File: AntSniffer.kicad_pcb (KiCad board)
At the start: 4 copper layers, 50.1 x 30.1 mm, 6 parts, among them CN1 X2026WRS-2X09D-LPSW, CN2 X2026WRS-2X09D-LPSW, J1 Conn_01x10_MountingPin

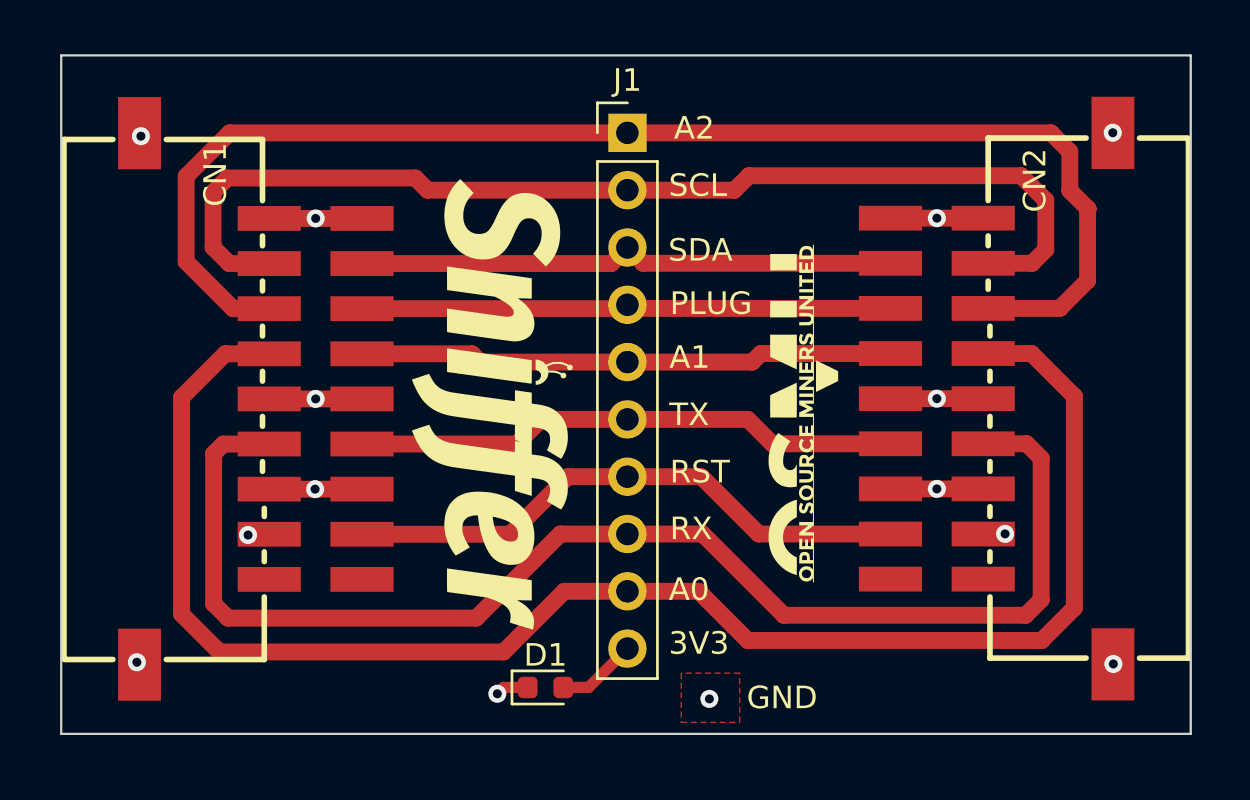
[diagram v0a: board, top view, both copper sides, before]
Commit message: switched to two layer board. added GND pin
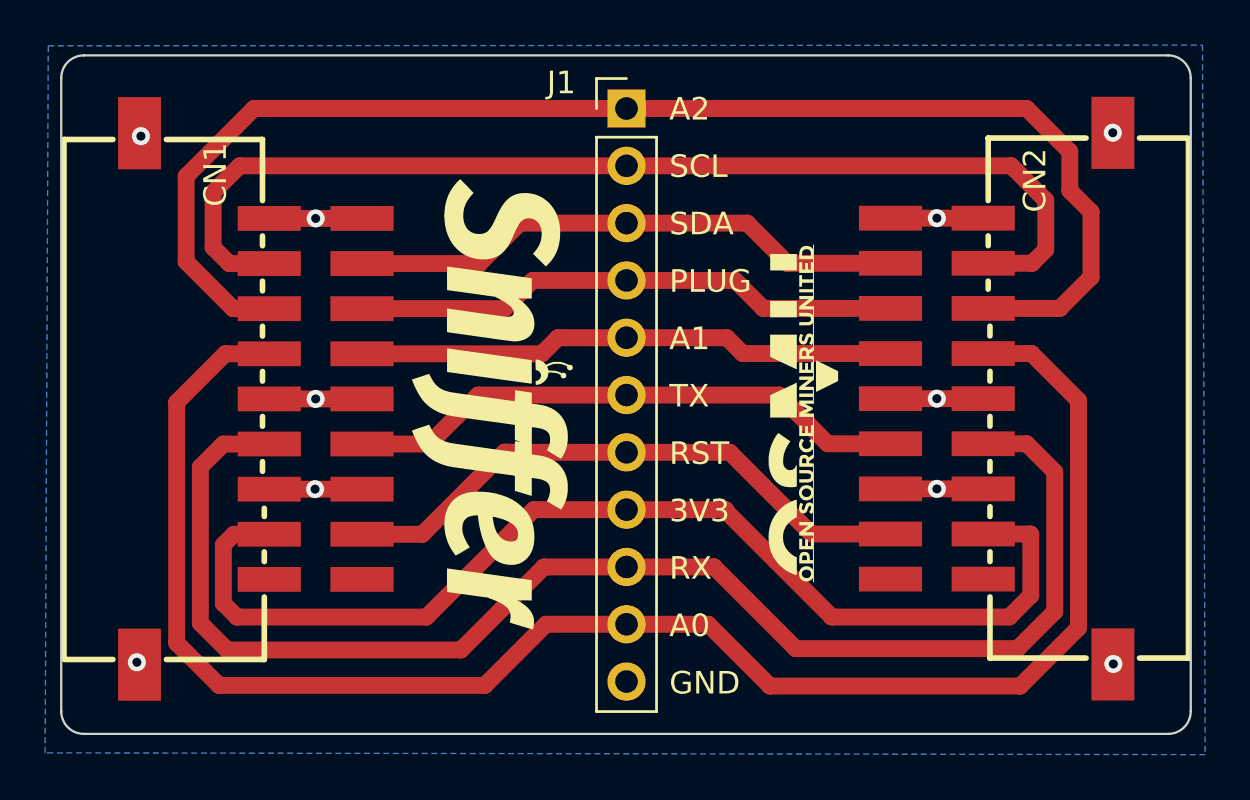
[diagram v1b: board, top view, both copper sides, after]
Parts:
- removed D1: LED, LED_SMD:LED_0603_1608Metric
- J1: footprint Connector_PinHeader_2.54mm:PinHeader_1x10_P2.54mm_Vertical -> Connector_PinHeader_2.54mm:PinHeader_1x11_P2.54mm_Vertical
- moved J1 1.08 mm to (168.5, 44.9)
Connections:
- J1 pad 10: /3V3 -> /A0
- J1 pad 8: /RX -> /3V3
- J1 pad 9: /A0 -> /RX
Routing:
- net /3V3: track 5.48 -> 52.0 mm, vias 2 -> 0
- net /RX: track 58.7 -> 62.4 mm
- net /A0: track 71.4 -> 74.9 mm
- net GND: track 26.5 -> 25.0 mm, vias 12 -> 10
- net /A2: track 59.8 -> 60.8 mm
- net /SDA: track 24.0 -> 24.9 mm
- net /RST: track 25.6 -> 26.4 mm
- net /TX: track 24.3 -> 25.2 mm
- net /PLUG: track 23.6 -> 24.5 mm
- added copper zone on B.Cu, net GND
- removed copper zone on In2.Cu, net /3V3
- removed copper zone on F.Cu, net GND
- removed copper zone on In1.Cu, net GND
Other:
- outline, holes or cut-outs redrawn
- copper layers 4 -> 2
- board text added: "Revision 2"
- board text added: "The AntSniffer"
- board text added: "by OSMU"
- board text removed: "Revision 1"
- board text removed: "The AntSniffer by OSMU"

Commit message: moved libraries local, updated render, generated BOM and manufacturing files
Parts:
- CN1, CN2: footprint EASYEDA2KICAD:CONN-SMD_X2026WRS-2X09D-LPSW -> antsniffer:CONN-SMD_X2026WRS-2X09D-LPSW
- G***: value LOGO -> SnifferLOGO; footprint LOGO -> antsniffer:SnifferLOGO
- Ge: footprint LOGO -> antsniffer:LOGO
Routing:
- net /3V3: track 52.0 -> 51.0 mm
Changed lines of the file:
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@@
     )
   )
-  (footprint "LOGO" (layer "F.Cu")
+  (footprint "antsniffer:LOGO" (layer "F.Cu")
     (at 176.50966 58.42 90)
     (attr board_only exclude_from_pos_files exclude_from_bom)
@@
       (stroke (width 0) (type solid)) (fill solid) (layer "F.SilkS"))
   )
-  (footprint "LOGO" (layer "F.Cu")
+  (footprint "antsniffer:SnifferLOGO" (layer "F.Cu")
     (at 162.6616 58.0136 -90)
     (attr board_only exclude_from_pos_files exclude_from_bom)
@@
         (effects (font (size 1.5 1.5) (thickness 0.3)))
     )
-    (fp_text value "LOGO" (at 0.75 0 90) (layer "F.SilkS") hide
+    (fp_text value "SnifferLOGO" (at 0.75 0 90) (layer "F.SilkS") hide
         (effects (font (size 1.5 1.5) (thickness 0.3)))
     )
@@
       (stroke (width 0) (type solid)) (fill solid) (layer "F.SilkS"))
   )
-  (footprint "EASYEDA2KICAD:CONN-SMD_X2026WRS-2X09D-LPSW" (layer "F.Cu")
+  (footprint "antsniffer:CONN-SMD_X2026WRS-2X09D-LPSW" (layer "F.Cu")
     (at 151.8848 57.7718 -90)
     (property "LCSC Part" "C718164")
@@
     (property "Sheetname" "")
     (attr smd)
-    (fp_text reference "CN1" (at -9.9436 1.5676 90) (layer "F.SilkS")
+    (fp_text reference "CN1" (at 9.6774 1.4693 -90) (layer "F.SilkS")
         (effects (font (size 1 1) (thickness 0.15)))
     )
-    (fp_text value "X2026WRS-2X09D-LPSW" (at 0 8.93 90) (layer "F.Fab")
+    (fp_text value "X2026WRS-2X09D-LPSW" (at 0 8.93 -90) (layer "F.Fab")
         (effects (font (size 1 1) (thickness 0.15)))
     )
-    (fp_text user "${REFERENCE}" (at 0 0 90) (layer "F.Fab")
+    (fp_text user "${REFERENCE}" (at 0 0 -90) (layer "F.Fab")
         (effects (font (size 1 1) (thickness 0.15)))
     )
@@
     (pad "20" smd rect (at -11.78 4.93 90) (size 3.2 1.9) (layers "F.Cu" "F.Paste" "F.Mask")
       (net 5 "GND") (pinfunction "20") (pintype "unspecified"))
-    (model "${EASYEDA2KICAD}/easyeda2kicad.3dshapes/CONN-SMD_X2026WRS-2X09D-LPSW.wrl"
+    (model "${KIPRJMOD}/3d/CONN-SMD_X2026WRS-2X09D-LPSW.wrl"
       (offset (xyz 0 -0.15 -0))
       (scale (xyz 1 1 1))
@@
     )
   )
-  (footprint "EASYEDA2KICAD:CONN-SMD_X2026WRS-2X09D-LPSW" (layer "F.Cu")
+  (footprint "antsniffer:CONN-SMD_X2026WRS-2X09D-LPSW" (layer "F.Cu")
     (at 185.1699 57.7596 90)
     (property "LCSC Part" "C718164")
@@
     (pad "20" smd rect (at -11.78 4.93 270) (size 3.2 1.9) (layers "F.Cu" "F.Paste" "F.Mask")
       (net 5 "GND") (pinfunction "20") (pintype "unspecified"))
-    (model "${EASYEDA2KICAD}/easyeda2kicad.3dshapes/CONN-SMD_X2026WRS-2X09D-LPSW.wrl"
+    (model "${KIPRJMOD}/3d/CONN-SMD_X2026WRS-2X09D-LPSW.wrl"
       (offset (xyz 0 -0.15 -0))
       (scale (xyz 1 1 1))
@@
   (segment (start 150.67 64.24) (end 150.67 66.837) (width 0.75) (layer "F.Cu") (net 4))
   (segment (start 159.67 67.44) (end 164.43 62.68) (width 0.75) (layer "F.Cu") (net 4))
-  (segment (start 184.3499 63.7596) (end 185.3128 63.7596) (width 0.75) (layer "F.Cu") (net 4))
   (segment (start 172.93 62.73) (end 172.93 62.68) (width 0.75) (layer "F.Cu") (net 4))
   (segment (start 151.1382 63.7718) (end 150.67 64.24) (width 0.75) (layer "F.Cu") (net 4))
